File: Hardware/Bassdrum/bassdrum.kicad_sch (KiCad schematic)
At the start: 0 parts

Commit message: Added untested op amp circuits for all three devices.
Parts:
- added C3: 1uF, symbol Device:C_Small
- added J1, J3: Esp32 socket, Connector_PinSocket_2.54mm:PinSocket_1x19_P2.54mm_Vertical, symbol Connector:Conn_01x19_Socket
- added MK1: Electret microphone, symbol Device:Microphone
- added R2: 1.5k?, symbol Device:R_Small
- added R7: 100k?, symbol Device:R_Small
- added R8: 500k, symbol Device:R_Small
- added R9: 500k?, symbol Device:R_Small
- added RV2: 1M?, symbol Device:R_Potentiometer_Trim
- added U2: MCP6002-xP, symbol Amplifier_Operational:MCP6002-xP
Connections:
- new net: C3.1, MK1.2 (+), R2.2
- new net: R8.2, R9.1, U2.3 (+)
- new net: U2.5 (+), U2.6 (-)
- new net: R7.2, RV2.2, RV2.3, U2.2 (-)
- new net: C3.2, R7.1
- new net +3.3V: J3.1 (Pin_1), R2.1, R9.2, U2.8 (V+)
- new net +5V: J3.19 (Pin_19)
- new net 0: J1.14 (Pin_14)
- new net 12: J3.13 (Pin_13)
- new net 13: J3.15 (Pin_15)
- new net 14: J3.12 (Pin_12)
- new net 15: J1.16 (Pin_16)
- new net 16: J1.12 (Pin_12)
- new net 17: J1.11 (Pin_11)
- new net 18: J1.9 (Pin_9)
- new net 19: J1.8 (Pin_8)
- new net 2: J1.15 (Pin_15)
- new net 21: J1.6 (Pin_6)
- new net 22: J1.3 (Pin_3)
- new net 23: J1.2 (Pin_2)
- new net 26: J3.10 (Pin_10)
- new net 27: J3.11 (Pin_11)
- new net 32: J3.7 (Pin_7)
- new net 33: J3.8 (Pin_8)
- new net 34: J3.5 (Pin_5)
- new net 35: J3.6 (Pin_6)
- new net 4: J1.13 (Pin_13)
- new net 5: J1.10 (Pin_10)
- new net CLK: J1.19 (Pin_19)
- new net CMD: J3.18 (Pin_18)
- new net D1: J1.17 (Pin_17)
- new net D2: J3.16 (Pin_16)
- new net D3: J3.17 (Pin_17)
- new net D9: J1.18 (Pin_18)
- new net DAC1: J3.9 (Pin_9)
- new net EN: J3.2 (Pin_2)
- new net GND: J1.1 (Pin_1), J1.7 (Pin_7), J3.14 (Pin_14), MK1.1 (-), R8.1, U2.4 (V-)
- new net RX: J1.5 (Pin_5)
- new net TX: J1.4 (Pin_4)
- new net VN: J3.4 (Pin_4)
- new net VP: J3.3 (Pin_3), RV2.1, U2.1
- no-connect marks 0 -> 1
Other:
- note added: "ESP32"

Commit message: added PDF of hardware. Very small (if any) hardware changes.
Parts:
- R7: value 100k? -> 50k?
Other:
- note added: "MULTICOMP PRO ABM-713-RC"

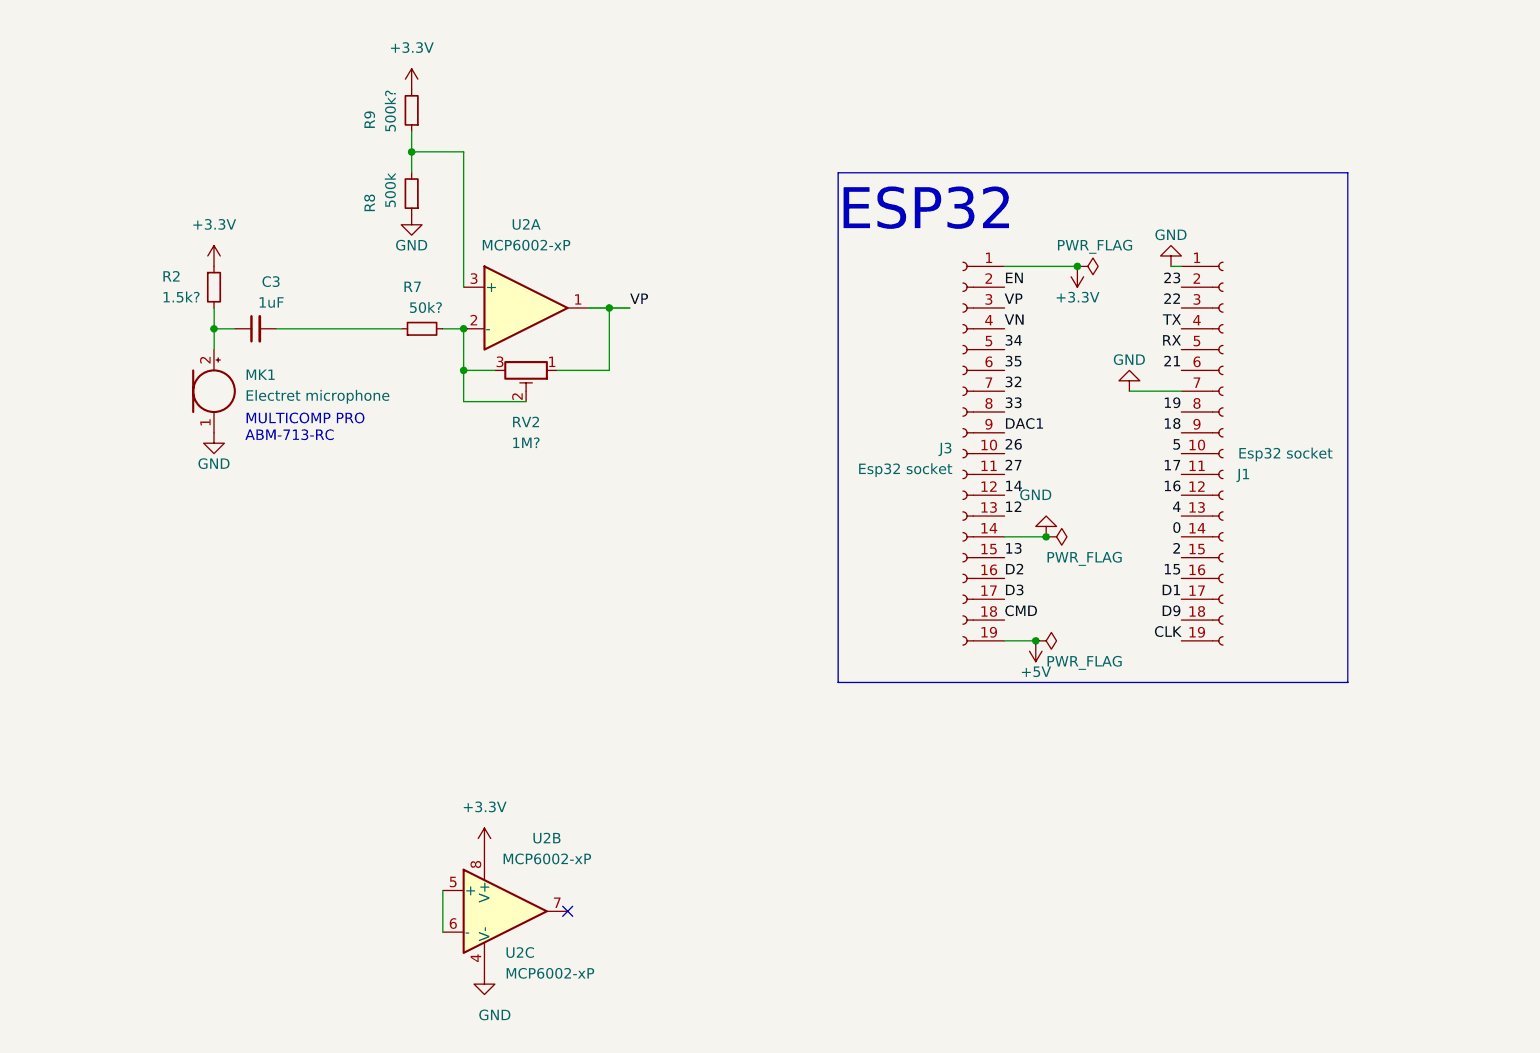
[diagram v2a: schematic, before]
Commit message: Greatly simplified the gateway/speaker module. Added a rectifying circuit and a comparator circuit to the bass drum module. Solidified some component values. Added decoupling capacitors to the schematic.
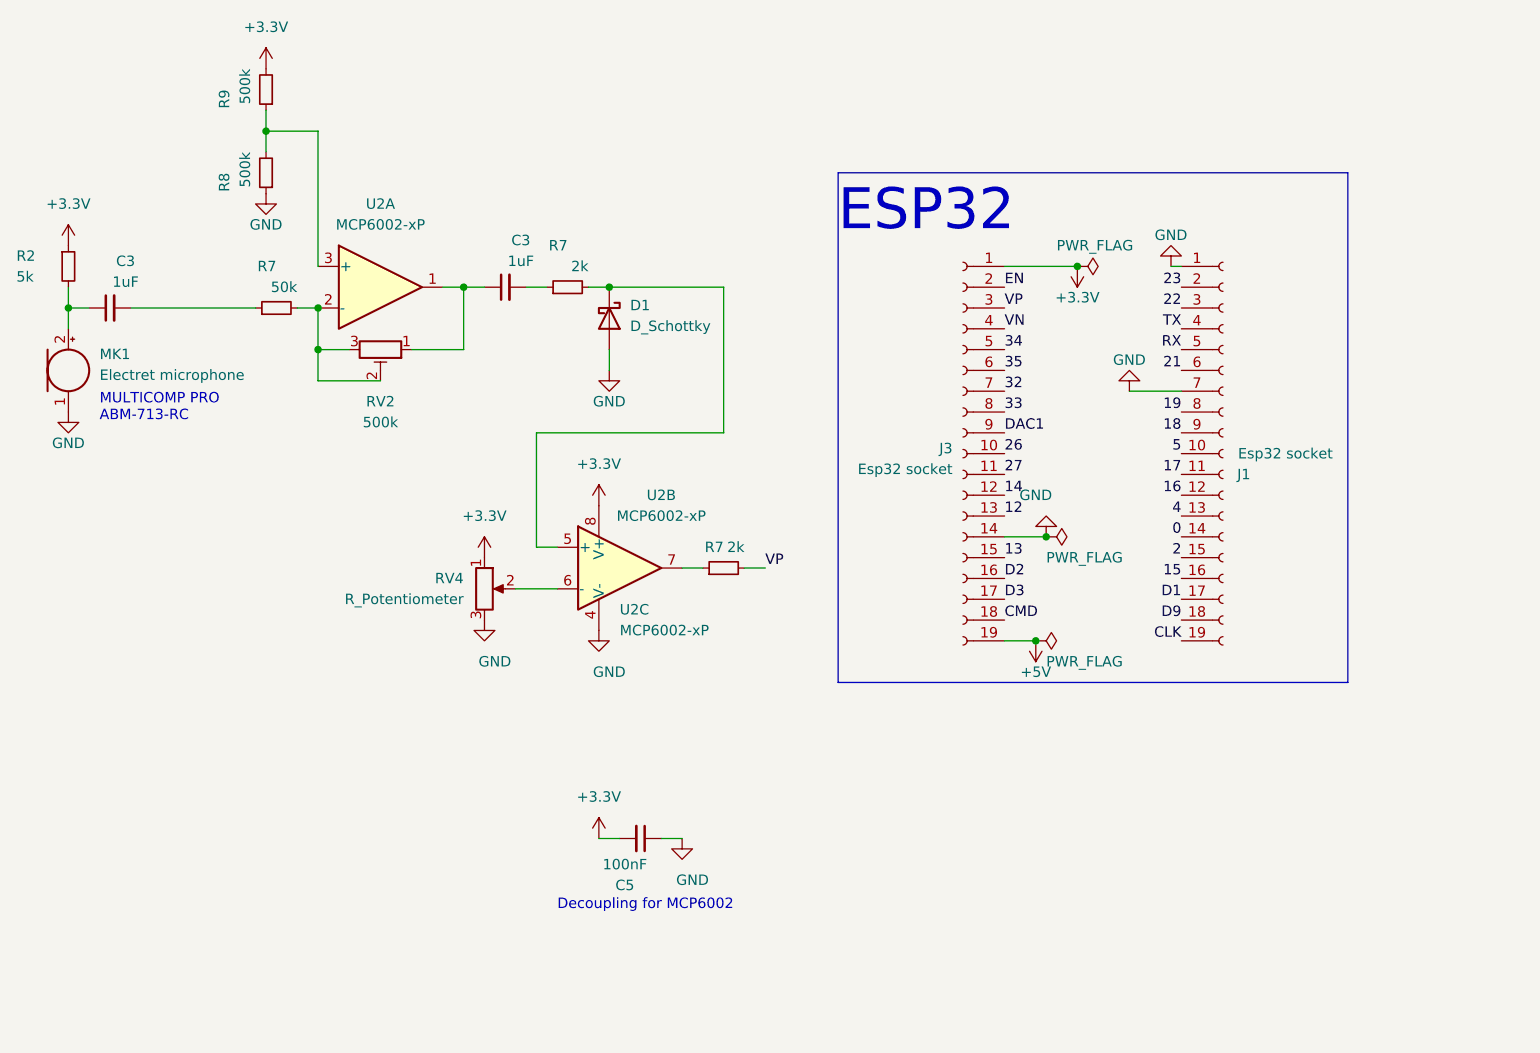
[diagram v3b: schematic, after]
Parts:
- added C3: 1uF, symbol Device:C_Small
- added C5: 100nF, symbol Device:C_Small
- added D1: D_Schottky, symbol Device:D_Schottky
- added R7 (x2): 2k, symbol Device:R_Small
- added RV4: R_Potentiometer, symbol Device:R_Potentiometer
- R2: value 1.5k? -> 5k
- R7: value 50k? -> 50k
- R9: value 500k? -> 500k
- RV2: value 1M? -> 500k
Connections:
- net +3.3V: now also C5.2, RV4.1
- net GND: now also C5.1, D1.2 (A), RV4.3
- net VP: now also R7.2; no longer RV2.1, U2.1
- net at U2.5 (+): now also D1.1 (K), R7.2; no longer U2.6 (-)
- net at U2.7: now also R7.1
- new net: RV4.2, U2.6 (-)
- new net: C3.1, RV2.1, U2.1
- new net: C3.2, R7.1
- no-connect marks 1 -> 0
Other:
- note added: "Decoupling for MCP6002"
- moved on the sheet: C3, MK1, R2, R7, R8, R9, RV2, U2A, U2B, U2C

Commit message: added batteries to the schematic.
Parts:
- added BT1: Battery, symbol Device:Battery
- added SW1: SW_SPST, symbol Switch:SW_SPST
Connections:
- net GND: now also BT1.2 (-)
- net +5V renamed Vin
- net Vin: now also SW1.2 (B)
- new net: BT1.1 (+), SW1.1 (A)
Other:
- moved on the sheet: C5
